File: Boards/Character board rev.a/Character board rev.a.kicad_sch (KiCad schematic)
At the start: 64 parts, among them J1 card edge, J2 character connector, Q1 2N6125, U1 6821, U1 R_Pack07, U13 7406, U14 74LS42, U15 LM741, U16 AH5012, U2 R_Pack07, U4 ULN2003A, U6 Board ID header, U9 LM741

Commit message: character card rev a done
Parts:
- R33: value 47.5KK -> 47.5K
- R33: value ? -> 120
- TP2: value GND -> +12
- TP2: value GND -> -12
- TP2: value GND -> 24
- TP2: value GND -> +5
- U1, U2: value R_Pack07 -> 2.2K
- renumbered D1 to CR1
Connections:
- net -12V: now also TP2.1
- net 12V: now also TP2.1
- net 24R: now also C25.1, J2.25 (Pin_25), J2.26 (Pin_26), U4.8 (GND), U4.8 (GND)
- net 24V: now also Q1.3 (E), RP1.14 (R3.2)
- net 5V: now also C25.1, C25.1, R33.1, RP1.10 (R7.2), RP1.11 (R6.2), RP1.12 (R5.2), RP1.13 (R4.2), RP1.15 (R2.2), RP1.16 (R1.2), RP1.9 (R8.2), TP2.1, U1.20 (VCC), U13.14 (VCC), U14.16 (VCC)
- net BA0: now also U1.36 (RS0)
- net BA1: now also U1.35 (RS1)
- net BS1: now also U6.1 (Pin_1)
- net BS10: now also U6.10 (Pin_10)
- net BS2: now also U6.2 (Pin_2)
- net BS3: now also U6.3 (Pin_3)
- net BS4: now also U6.4 (Pin_4)
- net BS5: now also U6.5 (Pin_5)
- net BS6: now also U6.6 (Pin_6)
- net BS7: now also U6.7 (Pin_7)
- net BS8: now also U6.8 (Pin_8)
- net BS9: now also U6.9 (Pin_9)
- net DBB0: now also U1.33 (D0)
- net DBB1: now also U1.32 (D1)
- net DBB2: now also U1.31 (D2)
- net DBB3: now also U1.30 (D3)
- net DBB4: now also U1.29 (D4)
- net DBB5: now also U1.28 (D5)
- net DBB6: now also U1.27 (D6)
- net DBB7: now also U1.26 (D7)
- net GND: now also C25.2, C25.2, C25.2, TP2.1, U1.1 (VSS), U13.7 (GND), U14.13 (A2), U14.8 (GND)
- net PHI2: now also U1.25 (ENABLE)
- net R/~{W}: now also U1.21 (R/~{W})
- net ~{MRST}: now also U1.34 (~{RESET})
- net A6out: now reaches DS1.1 (K)
- net A6out: now also J2.14 (Pin_14), U4.16 (O1)
- net at DS1.2 (A): now also U1.3 (R3.1)
- net B1out: now reaches DS1.1 (K)
- net B1out: now also J2.11 (Pin_11), U4.14 (O3)
- net at DS1.2 (A): now also U2.12 (R3.2)
- net at C25.1: now also R33.2; no longer R33.2
- net A1out: now reaches DS1.1 (K)
- net A1out: now also J2.19 (Pin_19), U4.11 (O6)
- net at DS1.2 (A): now also U1.6 (R6.1)
- net B4out: now reaches DS1.1 (K)
- net B4out: now also J2.8 (Pin_8), U4.11 (O6)
- net at DS1.2 (A): now also U2.9 (R6.2)
- net PA6: now reaches U4.1 (I1)
- net PA6: now also U1.8 (PA6)
- net A0out: now reaches U4.10 (O7)
- net A0out: now also DS1.1 (K), J2.20 (Pin_20)
- net A2out: now reaches U4.12 (O5)
- net A2out: now also DS1.1 (K), J2.18 (Pin_18)
- net A3out: now reaches U4.13 (O4)
- net A3out: now also DS1.1 (K), J2.17 (Pin_17)
- net A4out: now reaches U4.14 (O3)
- net A4out: now also DS1.1 (K), J2.16 (Pin_16)
- net A5out: now reaches U4.15 (O2)
- net A5out: now also DS1.1 (K), J2.15 (Pin_15)
- net PA5: now reaches U4.2 (I2)
- net PA5: now also U1.7 (PA5)
- net PA4: now reaches U4.3 (I3)
- net PA4: now also U1.6 (PA4)
- net PA3: now reaches U4.4 (I4)
- net PA3: now also U1.5 (PA3)
- net PA2: now reaches U4.5 (I5)
- net PA2: now also U1.4 (PA2)
- net PA1: now reaches U4.6 (I6)
- net PA1: now also U1.3 (PA1)
- net PA0: now reaches U4.7 (I7)
- net PA0: now also U1.2 (PA0)
- net 24Vout: now reaches U4.9 (COM)
- net 24Vout: now also F1.2, J2.21 (Pin_21), J2.22 (Pin_22), J2.23 (Pin_23), J2.24 (Pin_24), TP2.1, U1.10 (R5.2), U1.11 (R4.2), U1.12 (R3.2), U1.13 (R2.2), U1.14 (R1.2), U1.8 (R7.2), U1.9 (R6.2), U2.1 (R1.1), U2.2 (R2.1), U2.3 (R3.1), U2.4 (R4.1), U2.5 (R5.1), U2.6 (R6.1), U2.7 (R7.1), U4.9 (COM)
- net 24Vpu: now reaches Q1.1 (B)
- net 24Vpu: now also R33.1, RP1.3 (R3.1)
- net at Q1.2 (C): now also C25.2, F1.1
- net at R33.1: now also R33.2, U9.2 (-)
- net 5Vpu: now reaches U13.12
- net 5Vpu: now also RP1.2 (R2.1), U13.11
- net CA2: now reaches U13.13
- net CA2: now also RP1.1 (R1.1), U1.39 (CA2)
- net PA7: now reaches U4.1 (I1)
- net PA7: now also U1.9 (PA7)
- net B5out: now reaches U4.10 (O7)
- net B5out: now also DS1.1 (K), J2.7 (Pin_7)
- net B3out: now reaches U4.12 (O5)
- net B3out: now also DS1.1 (K), J2.9 (Pin_9)
- net B2out: now reaches U4.13 (O4)
- net B2out: now also DS1.1 (K), J2.10 (Pin_10)
- net B0out: now reaches U4.15 (O2)
- net B0out: now also DS1.1 (K), J2.12 (Pin_12)
- net A7out: now reaches U4.16 (O1)
- net A7out: now also DS1.1 (K), J2.13 (Pin_13)
- net PB0: now reaches U4.2 (I2)
- net PB0: now also U1.10 (PB0)
- net PB1: now reaches U4.3 (I3)
- net PB1: now also U1.11 (PB1)
- net PB2: now reaches U4.4 (I4)
- net PB2: now also U1.12 (PB2)
- net PB3: now reaches U4.5 (I5)
- net PB3: now also U1.13 (PB3)
- net PB4: now reaches U4.6 (I6)
- net PB4: now also U1.14 (PB4)
- net PB5: now reaches U4.7 (I7)
- net PB5: now also U1.15 (PB5)
- net at R33.1, R34.1: no longer U9.2 (-)
- net at U14.1 (0): now also RP1.8 (R8.1), U16.2
- net CB2: now reaches U14.12 (A3)
- net CB2: now also U1.19 (CB2)
- net PB7: now reaches U14.14 (A1)
- net PB7: now also U1.17 (PB7)
- net PB6: now reaches U14.15 (A0)
- net PB6: now also U1.16 (PB6)
- net at U14.2 (1): now also RP1.7 (R7.1), U16.7
- net at U14.3 (2): now also RP1.6 (R6.1), U16.10
- net at U14.4 (3): now also RP1.5 (R5.1), U16.15
- net at U2.10 (R5.2): now also DS1.2 (A)
- net at U2.11 (R4.2): now also DS1.2 (A)
- net at U2.13 (R2.2): now also DS1.2 (A)
- net at U2.14 (R1.2): now also DS1.2 (A)
- net at U2.8 (R7.2): now also DS1.2 (A)
- net at DS1.2 (A): now also U1.1 (R1.1)
- net at C25.1: now also R33.2, U13.10
- net at U1.2 (R2.1): now also DS1.2 (A)
- net at U1.4 (R4.1): now also DS1.2 (A)
- net at U1.5 (R5.1): now also DS1.2 (A)
- net at U1.7 (R7.1): now also DS1.2 (A)
- net CS: now reaches RP1.4 (R4.1)
- net CS: now also U1.22 (CS0), U1.24 (CS1)
- net at U6.14 (Pin_14): now also R33.2, U1.23 (~{CS2})
- no-connect marks 69 -> 92
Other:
- moved on the sheet: C1, C25, CR1, DS1, F1, J1, J2, Q1, R33, R34, RP1, TP2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

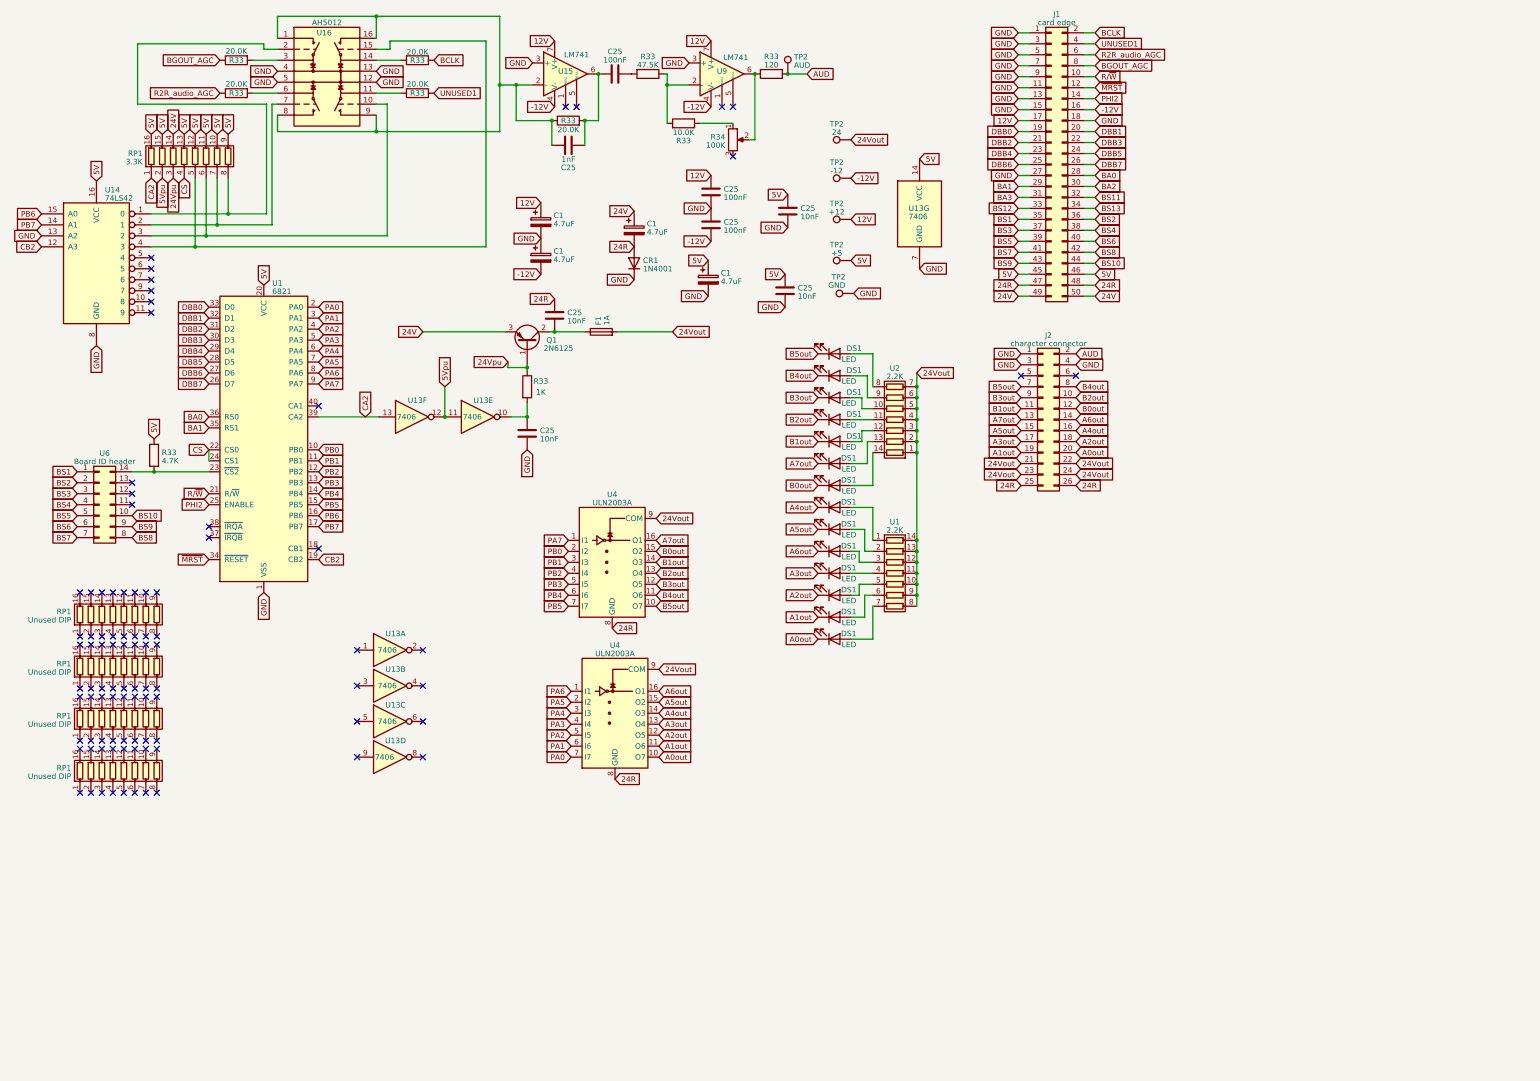
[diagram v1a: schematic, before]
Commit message: revised schematic to more match paper one
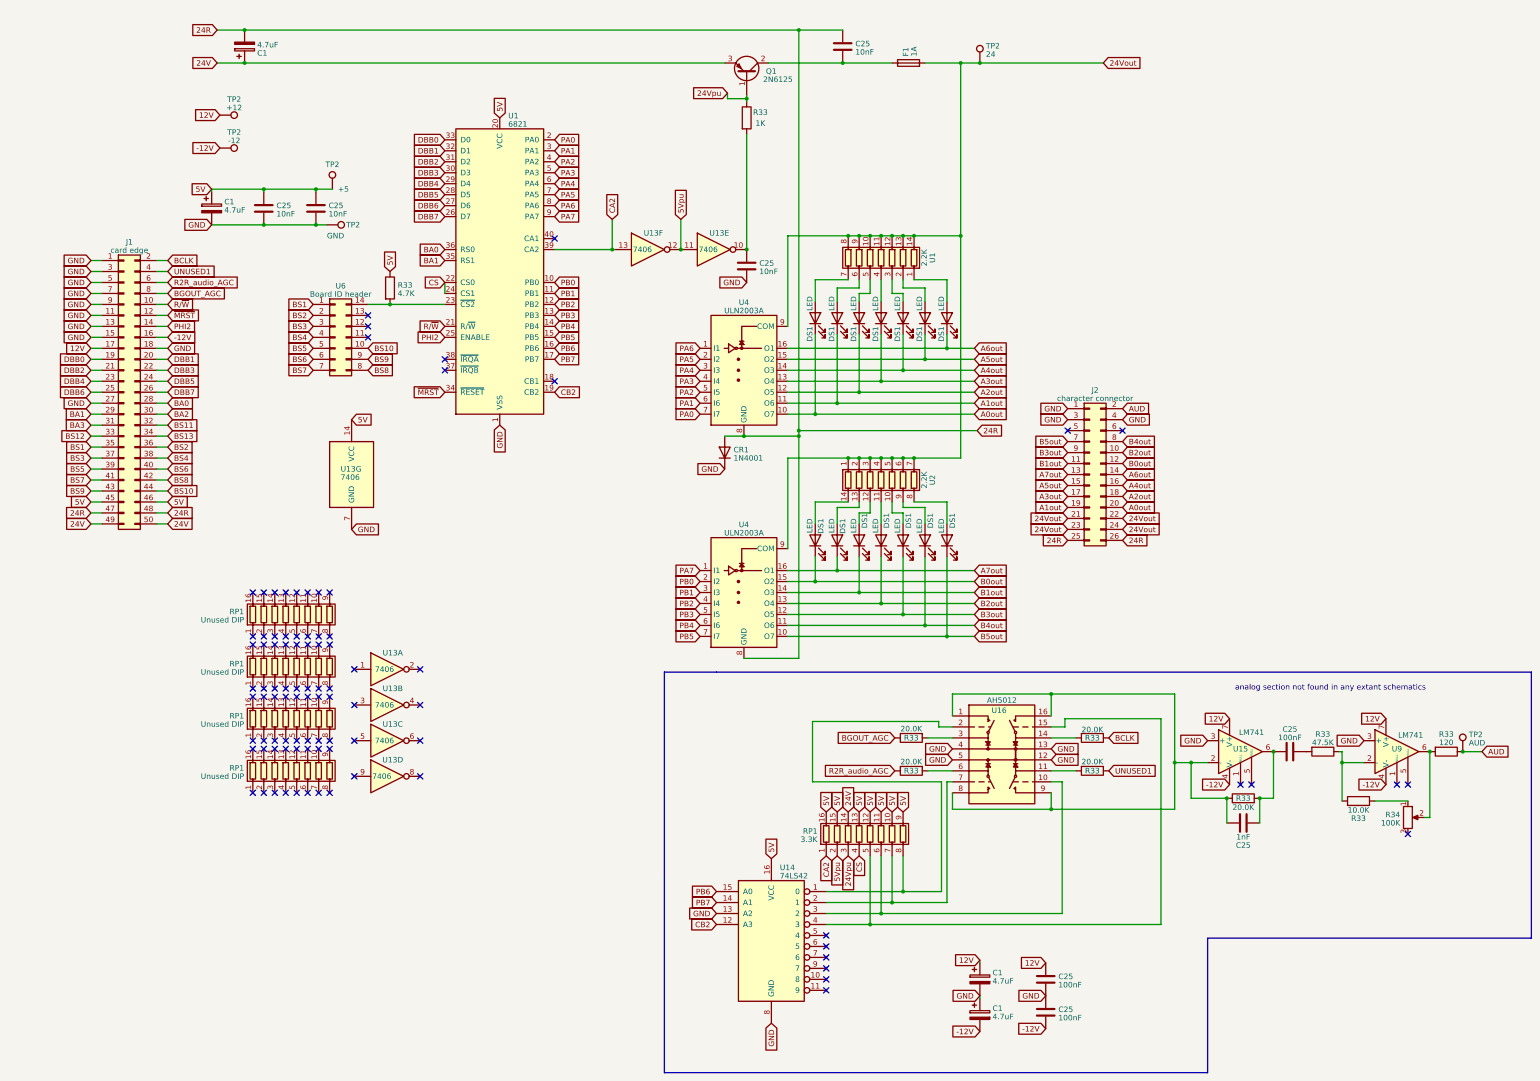
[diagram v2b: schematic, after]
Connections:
- net A4out: now also DS1.1 (K); no longer DS1.1 (K)
- net A6out: now also DS1.1 (K); no longer DS1.1 (K)
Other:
- note added: "analog section not found in any extant schematics"
- moved on the sheet: C1, C25, CR1, DS1, F1, J1, J2, Q1, R33, R34, RP1, TP2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

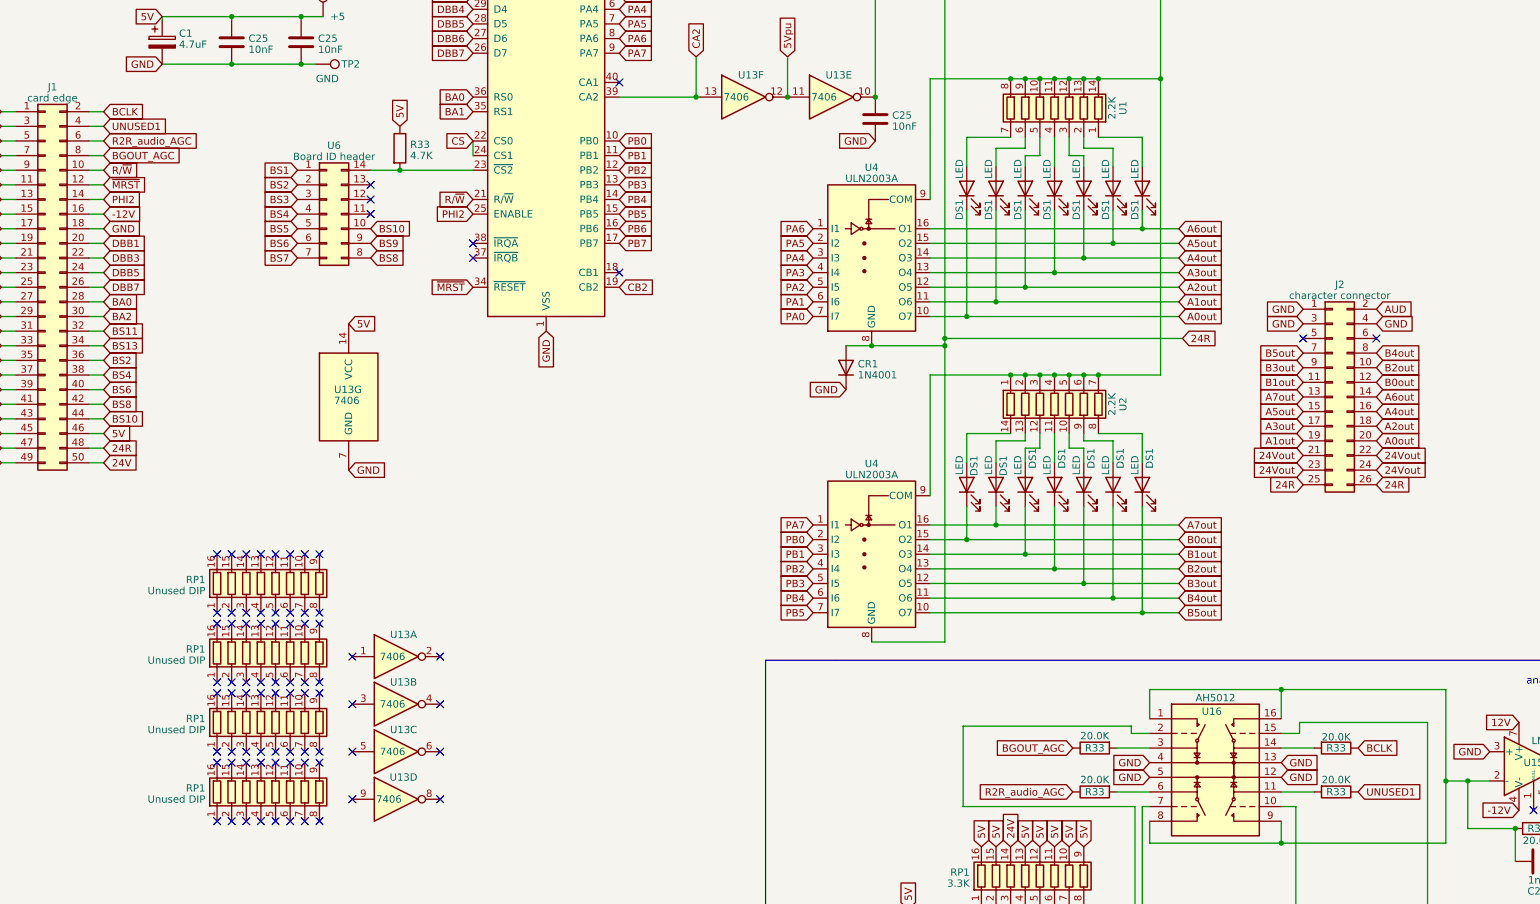
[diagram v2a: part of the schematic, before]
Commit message: revised all net names to reflect new information about 4 channel audio system
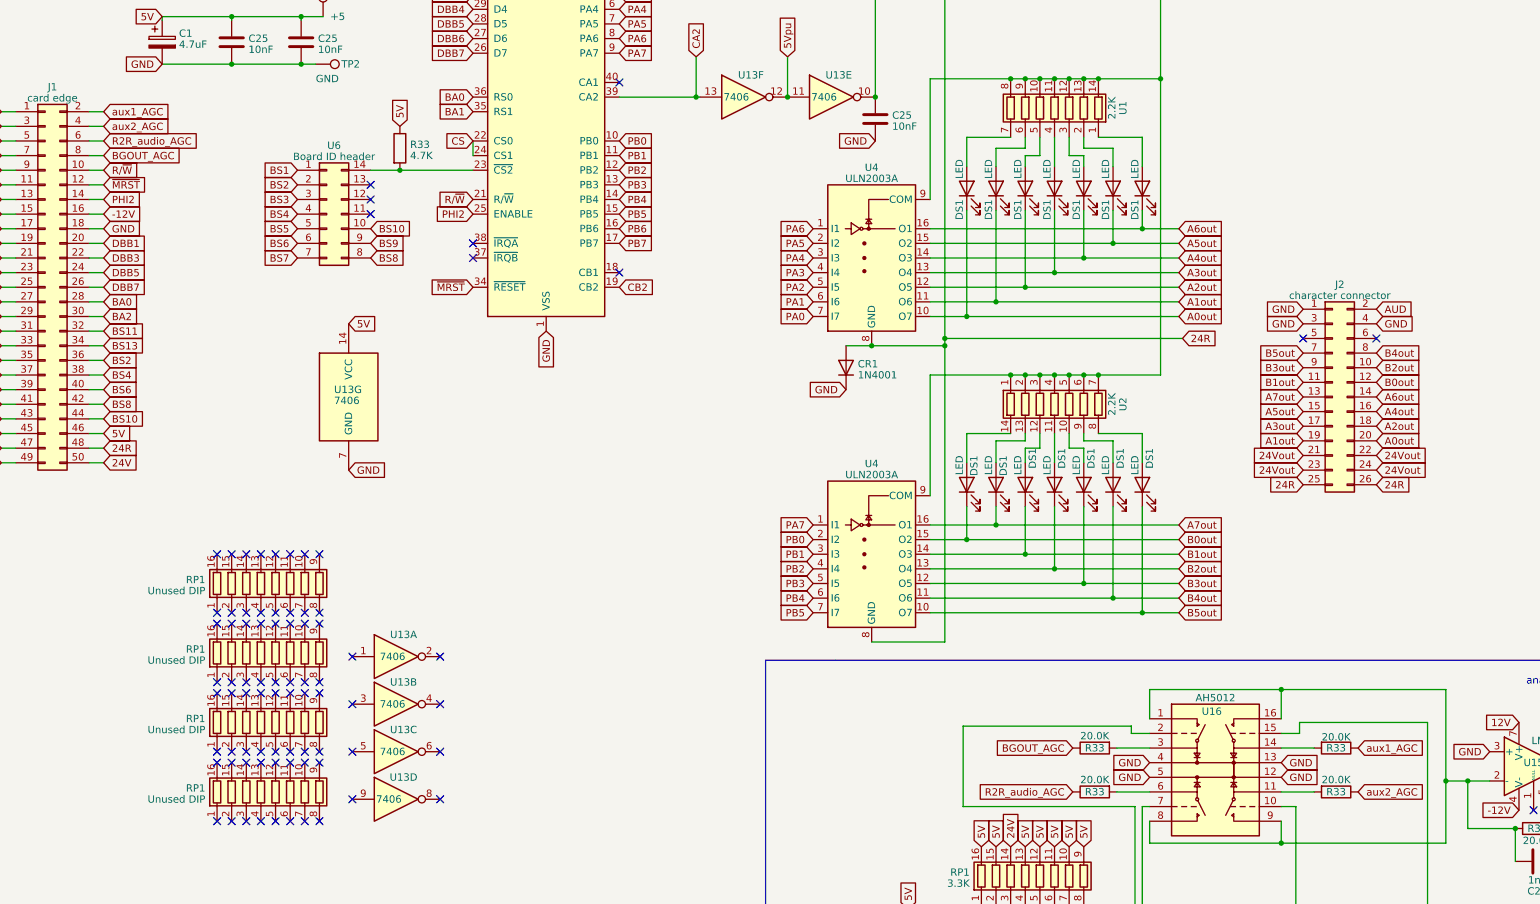
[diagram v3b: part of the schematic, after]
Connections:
- net BCLK renamed aux1_AGC
- net UNUSED1 renamed aux2_AGC
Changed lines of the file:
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@@
     (effects (font (size 1.27 1.27)) (justify left bottom))
   )
-  (global_label "BCLK" (shape input) (at 48.895 72.39 0) (fields_autoplaced)
-    (effects (font (size 1.27 1.27)) (justify left))
-    (property "Intersheetrefs" "${INTERSHEET_REFS}" (at 56.6389 72.39 0)
+  (global_label "aux1_AGC" (shape input) (at 48.895 72.39 0) (fields_autoplaced)
+    (effects (font (size 1.27 1.27)) (justify left))
+    (property "Intersheetrefs" "${INTERSHEET_REFS}" (at 60.9326 72.39 0)
       (effects (font (size 1.27 1.27)) (justify left) hide)
     )
@@
     )
   )
-  (global_label "UNUSED1" (shape input) (at 48.895 74.93 0) (fields_autoplaced)
-    (effects (font (size 1.27 1.27)) (justify left))
-    (property "Intersheetrefs" "${INTERSHEET_REFS}" (at 60.6303 74.93 0)
+  (global_label "aux2_AGC" (shape input) (at 48.895 74.93 0) (fields_autoplaced)
+    (effects (font (size 1.27 1.27)) (justify left))
+    (property "Intersheetrefs" "${INTERSHEET_REFS}" (at 60.9326 74.93 0)
       (effects (font (size 1.27 1.27)) (justify left) hide)
     )
@@
     )
   )
-  (global_label "UNUSED1" (shape input) (at 266.7 190.5 0) (fields_autoplaced)
-    (effects (font (size 1.27 1.27)) (justify left))
-    (property "Intersheetrefs" "${INTERSHEET_REFS}" (at 278.4353 190.5 0)
+  (global_label "aux2_AGC" (shape input) (at 266.7 190.5 0) (fields_autoplaced)
+    (effects (font (size 1.27 1.27)) (justify left))
+    (property "Intersheetrefs" "${INTERSHEET_REFS}" (at 278.7376 190.5 0)
       (effects (font (size 1.27 1.27)) (justify left) hide)
     )
@@
     )
   )
-  (global_label "BCLK" (shape input) (at 266.7 182.88 0) (fields_autoplaced)
-    (effects (font (size 1.27 1.27)) (justify left))
-    (property "Intersheetrefs" "${INTERSHEET_REFS}" (at 274.4439 182.88 0)
-      (effects (font (size 1.27 1.27)) (justify left) hide)
-    )
+  (global_label "aux1_AGC" (shape input) (at 266.7 182.88 0) (fields_autoplaced)
+    (effects (font (size 1.27 1.27)) (justify left))
+    (property "Intersheetrefs" "${INTERSHEET_REFS}" (at 278.7376 182.88 0)
+      (effects (font (size 1.27 1.27)) (justify left) hide)
+    )
